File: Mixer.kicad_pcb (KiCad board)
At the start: 2 copper layers, 102 x 69.2 mm, 54 parts, among them J1 JST XH, J10 JST XH, J11 JST XH, J12 Conn_01x03_Female, J2 JST XH, J3 JST XH, J4 JST XH, J5 JST XH, J6 JST XH, J7 JST XH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

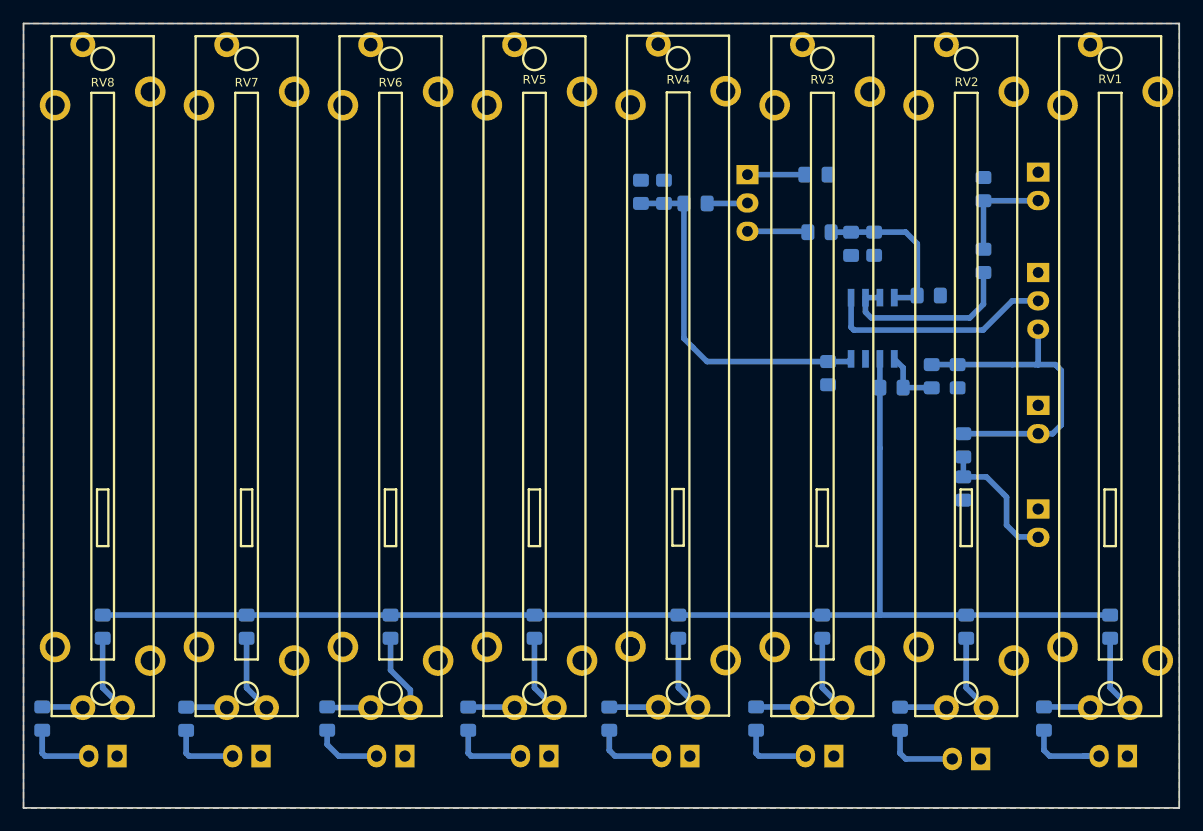
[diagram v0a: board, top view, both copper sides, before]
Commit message: bugfix after prototype build
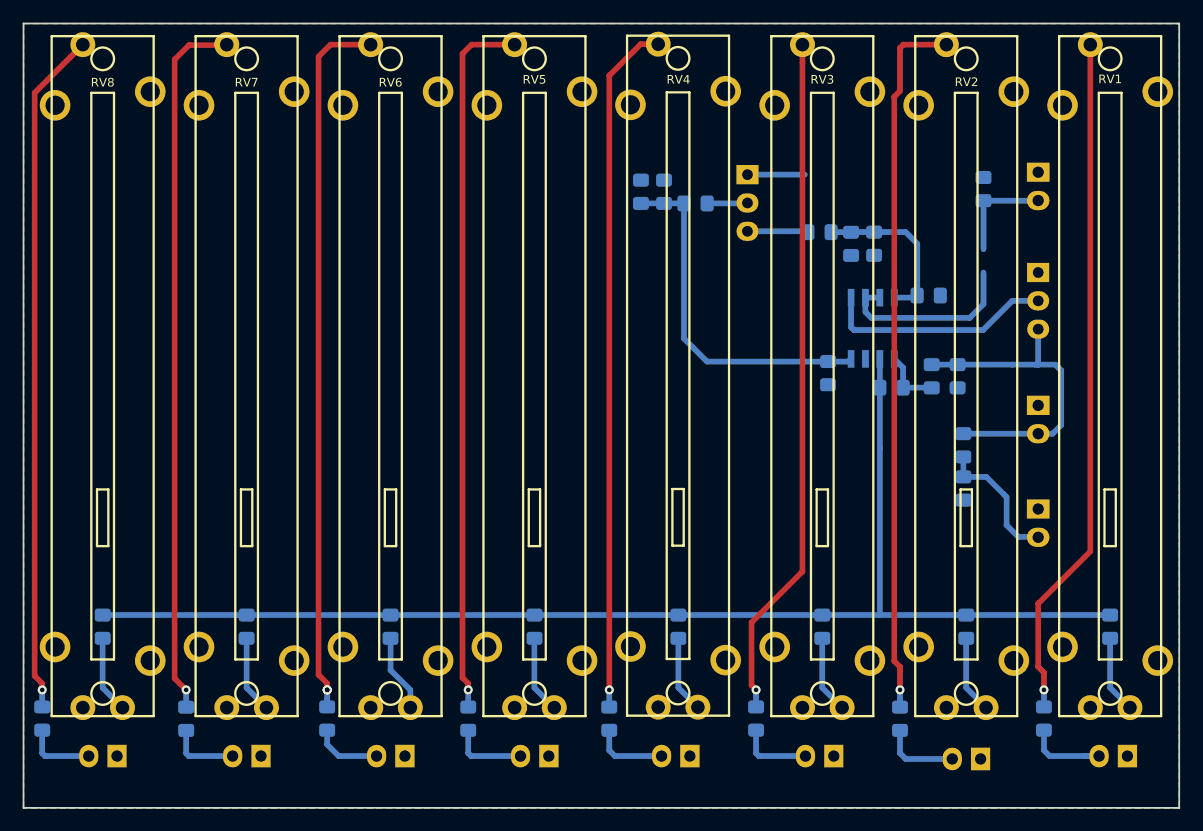
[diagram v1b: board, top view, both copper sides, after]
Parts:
- removed C12: 10u, Capacitor_SMD:C_0805_2012Metric_Pad1.15x1.40mm_HandSolder
- removed L3: LQM21DN220N00L, Resistor_SMD:R_0805_2012Metric_Pad1.15x1.40mm_HandSolder
- R10: value 1M -> 10K
- R13: value 1M -> 120R
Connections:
- J12 pad 1: Net-(J12-Pad1) -> GND
- R13 pad 1: GND -> Net-(R13-Pad1)
- RV1 pad 1: Net-(C1-Pad1) -> GND
- RV1 pad 3: GND -> Net-(C1-Pad1)
- RV2 pad 1: Net-(C2-Pad1) -> GND
- RV2 pad 3: GND -> Net-(C2-Pad1)
- RV3 pad 1: Net-(C3-Pad1) -> GND
- RV3 pad 3: GND -> Net-(C3-Pad1)
- RV4 pad 1: Net-(C4-Pad1) -> GND
- RV4 pad 3: GND -> Net-(C4-Pad1)
- RV5 pad 1: Net-(C5-Pad1) -> GND
- RV5 pad 3: GND -> Net-(C5-Pad1)
- RV6 pad 1: Net-(C6-Pad1) -> GND
- RV6 pad 3: GND -> Net-(C6-Pad1)
- RV7 pad 1: Net-(C7-Pad1) -> GND
- RV7 pad 3: GND -> Net-(C7-Pad1)
- RV8 pad 1: Net-(C8-Pad1) -> GND
- RV8 pad 3: GND -> Net-(C8-Pad1)
- U1 pad 6: Net-(C12-Pad2) -> Net-(R13-Pad1)
- U1 pad 7: Net-(C12-Pad2) -> Net-(R13-Pad1)
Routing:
- net Net-(C7-Pad1): track 3.60 -> 62.7 mm, vias 0 -> 1
- net Net-(C6-Pad1): track 3.86 -> 62.8 mm, vias 0 -> 2
- net Net-(C2-Pad1): track 4.11 -> 62.8 mm, vias 0 -> 1
- net Net-(C5-Pad1): track 4.11 -> 62.8 mm, vias 0 -> 1
- net Net-(C4-Pad1): track 4.32 -> 61.2 mm, vias 0 -> 1
- net Net-(C8-Pad1): track 3.61 -> 60.5 mm, vias 0 -> 1
- net Net-(C1-Pad1): track 4.12 -> 60.6 mm, vias 0 -> 1
- net Net-(C3-Pad1): track 4.12 -> 60.5 mm, vias 0 -> 1
- net Net-(R13-Pad1): track 0.00 -> 16.5 mm
- net Net-(C12-Pad2): track 16.5 -> 0.00 mm
- net GND: track 0.00 -> 5.49 mm
- net Net-(J12-Pad1): track 5.06 -> 0.00 mm
